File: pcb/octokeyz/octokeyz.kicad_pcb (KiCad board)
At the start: 2 copper layers, 84.6 x 36.3 mm, 30 parts, among them J1 USB, J2 ISP Programming, SW1 SW_Push, SW2 SW_Push, SW3 SW_Push, SW4 SW_Push, SW5 SW_Push, SW6 SW_Push, SW7 SW_Push, SW8 SW_Push, U1 ATtiny4313-P, Y1 20MHz

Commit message: pcb: octokeyz: revision 20240601
minor changes.
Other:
- board text added: "+5V OUT. ONLY!"
- board text added: "GND"
- board text added: "ISP"
- board text added: "MISO"
- board text added: "MOSI"
- board text added: "RESET"
- board text added: "SCK"
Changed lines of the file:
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@@
 	(title_block
 		(title "octokeyz")
-		(date "2024-05-30")
-		(rev "20240530")
+		(date "2024-06-01")
+		(rev "20240601")
 		(comment 3 "Released under CERN Open Hardware Licence Version 2 - Strongly Reciprocal")
 		(comment 4 "Designed by: Rafael G. Martins")
@@
 			)
 		)
-		(fp_text user "K"
-			(at 0 -1.8 90)
+		(fp_text user "${REFERENCE}"
+			(at 4.11 0 90)
 			(layer "F.Fab")
 			(effects
 				(font
-					(size 1 1)
-					(thickness 0.15)
+					(size 0.8 0.8)
+					(thickness 0.12)
 				)
 			)
 		)
-		(fp_text user "${REFERENCE}"
-			(at 4.11 0 90)
+		(fp_text user "K"
+			(at 0 -1.8 90)
 			(layer "F.Fab")
 			(effects
 				(font
-					(size 0.8 0.8)
-					(thickness 0.12)
+					(size 1 1)
+					(thickness 0.15)
 				)
 			)
@@
 		(tags "Through hole angled pin header THT 1x06 2.54mm single row")
 		(property "Reference" "J2"
-			(at 4 3.2 180)
+			(at 2.724 3.175 180)
 			(layer "B.SilkS")
 			(effects
@@
 					(thickness 0.15)
 				)
-				(justify mirror)
+				(justify left mirror)
 			)
 		)
@@
 			(layer "B.Fab")
 		)
-		(fp_text user "MOSI"
-			(at 7.95 -11.85 0)
-			(unlocked yes)
-			(layer "B.SilkS")
-			(effects
-				(font
-					(size 0.6 0.6)
-					(thickness 0.15)
-				)
-				(justify left mirror)
-			)
-		)
-		(fp_text user "GND"
-			(at 8.25 -1.65 0)
-			(unlocked yes)
-			(layer "B.SilkS")
-			(effects
-				(font
-					(size 0.6 0.6)
-					(thickness 0.15)
-				)
-				(justify left mirror)
-			)
-		)
-		(fp_text user "+5V"
-			(at 8.15 0.9 0)
-			(unlocked yes)
-			(layer "B.SilkS")
-			(effects
-				(font
-					(size 0.6 0.6)
-					(thickness 0.15)
-				)
-				(justify left mirror)
-			)
-		)
-		(fp_text user "SCK"
-			(at 8.3 -6.75 0)
-			(unlocked yes)
-			(layer "B.SilkS")
-			(effects
-				(font
-					(size 0.6 0.6)
-					(thickness 0.15)
-				)
-				(justify left mirror)
-			)
-		)
-		(fp_text user "RESET"
-			(at 7.35 -9.3 0)
-			(unlocked yes)
-			(layer "B.SilkS")
-			(effects
-				(font
-					(size 0.6 0.6)
-					(thickness 0.15)
-				)
-				(justify left mirror)
-			)
-		)
-		(fp_text user "ISP"
-			(at 3.15 2.05 0)
-			(unlocked yes)
-			(layer "B.SilkS")
-			(effects
-				(font
-					(size 0.6 0.6)
-					(thickness 0.15)
-				)
-				(justify left mirror)
-			)
-		)
-		(fp_text user "MISO"
-			(at 7.95 -4.2 0)
-			(unlocked yes)
-			(layer "B.SilkS")
-			(effects
-				(font
-					(size 0.6 0.6)
-					(thickness 0.15)
-				)
-				(justify left mirror)
-			)
-		)
 		(fp_text user "${REFERENCE}"
 			(at 2.77 -6.35 -90)
@@
 		(layer "Edge.Cuts")
 	)
+	(gr_text "+5V\nOUT. ONLY!"
+		(at 113.665 73.787 0)
+		(layer "B.SilkS")
+		(effects
+			(font
+				(size 0.6 0.6)
+				(thickness 0.15)
+			)
+			(justify right mirror)
+		)
+	)
+	(gr_text "MISO"
+		(at 113.665 79.375 0)
+		(layer "B.SilkS")
+		(effects
+			(font
+				(size 0.6 0.6)
+				(thickness 0.15)
+			)
+			(justify right mirror)
+		)
+	)
+	(gr_text "RESET"
+		(at 113.665 84.455 0)
+		(layer "B.SilkS")
+		(effects
+			(font
+				(size 0.6 0.6)
+				(thickness 0.15)
+			)
+			(justify right mirror)
+		)
+	)
+	(gr_text "SCK"
+		(at 113.665 81.915 0)
+		(layer "B.SilkS")
+		(effects
+			(font
+				(size 0.6 0.6)
+				(thickness 0.15)
+			)
+			(justify right mirror)
+		)
+	)
+	(gr_text "ISP"
+		(at 121.158 73.152 0)
+		(layer "B.SilkS")
+		(effects
+			(font
+				(size 0.6 0.6)
+				(thickness 0.15)
+			)
+			(justify left mirror)
+		)
+	)
 	(gr_text "Rev: ${REVISION}"
 		(at 160.909 98.425 0)
@@
 		)
 	)
+	(gr_text "MOSI"
+		(at 113.665 86.995 0)
+		(layer "B.SilkS")
+		(effects
+			(font
+				(size 0.6 0.6)
+				(thickness 0.15)
+			)
+			(justify right mirror)
+		)
+	)
+	(gr_text "GND"
+		(at 113.665 76.835 0)
+		(layer "B.SilkS")
+		(effects
+			(font
+				(size 0.6 0.6)
+				(thickness 0.15)
+			)
+			(justify right mirror)
+		)
+	)

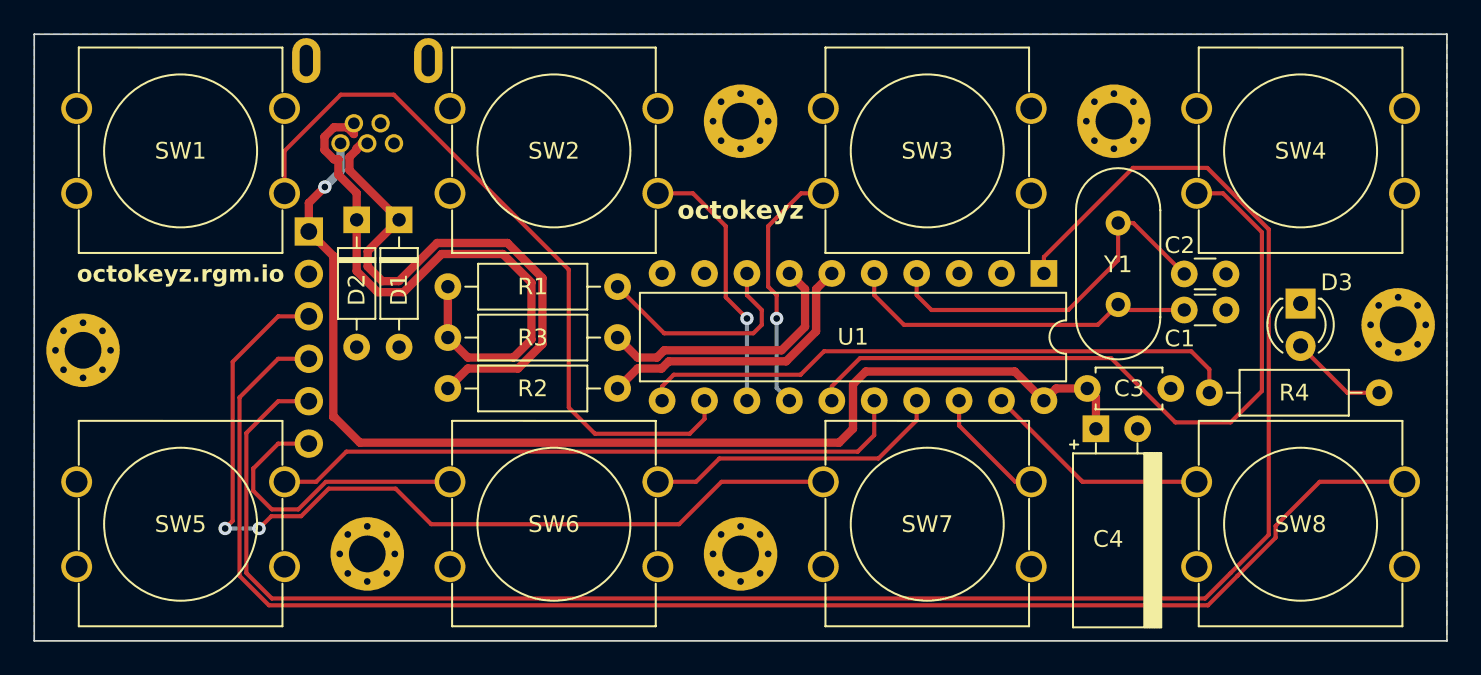
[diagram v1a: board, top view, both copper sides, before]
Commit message: pcb: octokeyz: revision 20240616
use stm32 instead of avr microcontroller. the prices are similar
nowadays, and it will allow us to have a single DFU-capable and
BSD-licensed firmware usable by all boards.

the board outline and the position of buttons and connectors is the
same, any existing cases should still fit correctly.
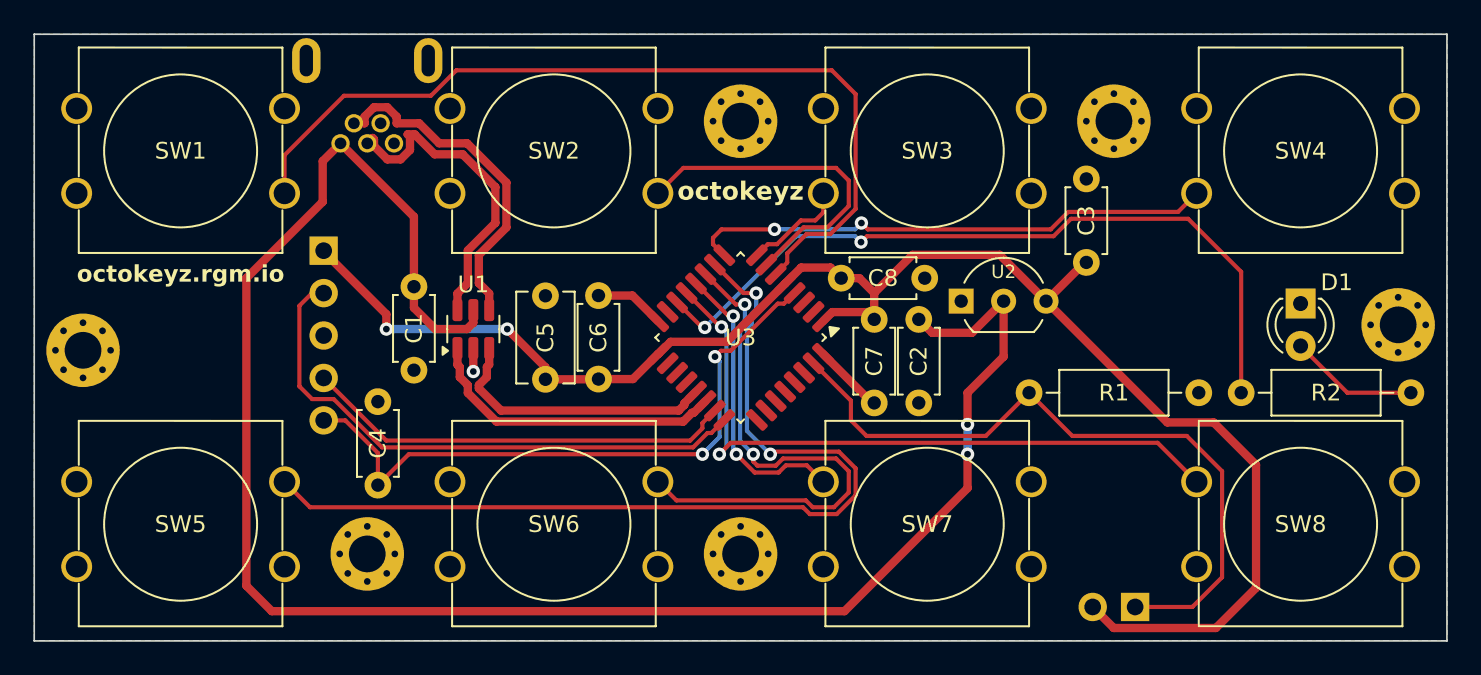
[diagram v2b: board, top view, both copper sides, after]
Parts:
- removed the D1 at (129.3, 74.5)
- removed D2: 3V6, Diode_THT:D_DO-35_SOD27_P7.62mm_Horizontal
- removed the R2 at (132.2, 84.6)
- removed R3: 68R, octokeyz:R_YAGEO_MFR-25FTE52_Horizontal
- removed Y1: 20MHz, Crystal:Crystal_HC49-4H_Vertical
- added C5: 10u, octokeyz:C_TDK_FA26, F.Cu at (138.0, 79.0)
- added C6: 100n, octokeyz:C_TDK_FA28, F.Cu at (141.2, 79.0)
- added C7: 100n, octokeyz:C_TDK_FA28, F.Cu at (157.7, 85.4)
- added C8: 100n, octokeyz:C_TDK_FA28, F.Cu at (160.8, 78.0)
- added JP1: BOOT, Connector_PinHeader_2.54mm:PinHeader_1x02_P2.54mm_Horizontal, B.Cu at (173.4, 97.7)
- added U2: MCP1700-3302E, Package_TO_SOT_THT:TO-92_Inline_Wide, F.Cu at (162.9, 79.4)
- added U3: STM32F042K6T6, Package_QFP:LQFP-32_7x7mm_P0.8mm, F.Cu at (149.7, 81.5)
- C1: value 22p -> 100n; footprint Capacitor_THT:C_Disc_D3.0mm_W1.6mm_P2.50mm -> octokeyz:C_TDK_FA28
- C2: value 22p -> 1u; footprint Capacitor_THT:C_Disc_D3.0mm_W1.6mm_P2.50mm -> octokeyz:C_TDK_FA28
- C3: value 100n -> 1u
- C4: value 10u -> 100n; footprint octokeyz:CP_Radial_D5.0mm_P2.50mm_Horizontal -> octokeyz:C_TDK_FA28
- D1: renamed from D3; value LED -> LED Green 3mm
- J1: value USB -> USB_B_Mini
- J2: value ISP Programming -> PIN H 5P; footprint Connector_PinHeader_2.54mm:PinHeader_1x06_P2.54mm_Horizontal -> Connector_PinHeader_2.54mm:PinHeader_1x05_P2.54mm_Horizontal
- R1: value 2k2 -> 10k
- R2: renamed from R4; value 22k -> 10k
- SW1, SW2, SW3, SW4, SW5, SW6, SW7, SW8: value SW_Push -> SPST 12mm
- U1: value ATtiny4313-P -> USBLC6-2SC6; footprint Package_DIP:DIP-20_W7.62mm -> Package_TO_SOT_SMD:SOT-23-6
- moved C1 48.8 mm to (130.2, 83.5), turned to 90 degrees
- moved C4 43.0 mm to (128.0, 85.4), turned to -90 degrees
- moved R1 35.4 mm to (167.0, 84.8)
- moved U1 34.3 mm to (133.7, 81.0), turned to 90 degrees
- moved C2 19.9 mm to (160.4, 85.4), turned to 90 degrees
- moved C3 13.5 mm to (170.4, 72.0), turned to -90 degrees
- moved R2 1.91 mm to (179.7, 84.8)
- moved J2 1.45 mm to (124.8, 76.3)
- moved REF** 0.06 mm to (183.3, 70.4)
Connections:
- C1 pad 2: Net-(U1-PA0/XTAL1) -> +5V
- C2 pad 2: Net-(U1-PA1/XTAL2) -> +5V
- C3 pad 2: +5V -> +3.3V
- C4 pad 1: +5V -> GND
- C4 pad 2: GND -> RESET
- J2 pad 1: +5V -> +3.3V
- J2 pad 2: GND -> SWCLK
- J2 pad 3: MISO -> GND
- J2 pad 4: SCK -> SWDIO
- R1 pad 1: /USB_CONN_D- -> Net-(JP1-A)
- R1 pad 2: USB_PULLUP -> GND
- SW1 pad 4: Net-(U1-PB0) -> KEY1
- SW2 pad 4: Net-(U1-PB1) -> KEY2
- SW3 pad 3: Net-(U1-PB2) -> KEY3
- SW4 pad 3: Net-(U1-PB3) -> KEY4
- SW5 pad 2: Net-(U1-PB4) -> KEY5
- SW6 pad 1: MOSI -> unconnected-(SW6-Pad1)
- SW6 pad 2: Net-(U1-PB5) -> KEY6
- SW7 pad 1: MISO -> KEY7
- SW7 pad 2: Net-(U1-PB6) -> unconnected-(SW7-Pad2)
- SW8 pad 1: Net-(U1-PB7) -> KEY8
- SW8 pad 2: SCK -> unconnected-(SW8-Pad2)
- U1 pad 1: RESET -> USB_D+
- U1 pad 2: unconnected-(U1-PD0-Pad2) -> GND
- U1 pad 3: unconnected-(U1-PD1-Pad3) -> USB_D-
- U1 pad 4: Net-(U1-PA1/XTAL2) -> /USB_CONN_D-
- U1 pad 5: Net-(U1-PA0/XTAL1) -> +5V
- U1 pad 6: USB_D+ -> /USB_CONN_D+
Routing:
- net +3.3V: track 0.00 -> 96.9 mm, vias 0 -> 2
- net SCK: track 89.5 -> 0.00 mm
- net RESET: track 112.6 -> 38.9 mm, vias 0 -> 2
- net KEY5: track 0.00 -> 56.3 mm, vias 0 -> 2
- net MISO: track 54.3 -> 0.00 mm, vias 2 -> 0
- net KEY1: track 0.00 -> 52.8 mm
- net Net-(U1-PB3): track 44.1 -> 0.00 mm
- net Net-(U1-PB0): track 43.8 -> 0.00 mm
- net Net-(JP1-A): track 0.00 -> 42.3 mm
- net KEY8: track 0.00 -> 40.7 mm, vias 0 -> 2
- net +5V: track 70.5 -> 110.6 mm, vias 1 -> 2
- net Net-(U1-PB4): track 38.5 -> 0.00 mm
- net SWCLK: track 0.00 -> 34.2 mm
- net KEY6: track 0.00 -> 33.0 mm, vias 0 -> 2
- net KEY4: track 0.00 -> 31.7 mm, vias 0 -> 2
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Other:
- board text added: "+3.3V OUT. ONLY!"
- board text added: "Boot to DFU"
- board text added: "SWCLK"
- board text added: "SWD"
- board text added: "SWDIO"
- board text removed: "+5V OUT. ONLY!"
- board text removed: "ISP"
- board text removed: "MISO"
- board text removed: "MOSI"
- board text removed: "SCK"

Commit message: pcb: added STM32F042K4T6 as microcontroller alternative
as this is a purely cosmetic change that doesn't affects the produced
boards I do not bumped revision number neither re-generated gerber
files.
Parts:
- U3: value STM32F042K6T6 -> STM32F042K4T6 or STM32F042K6T6

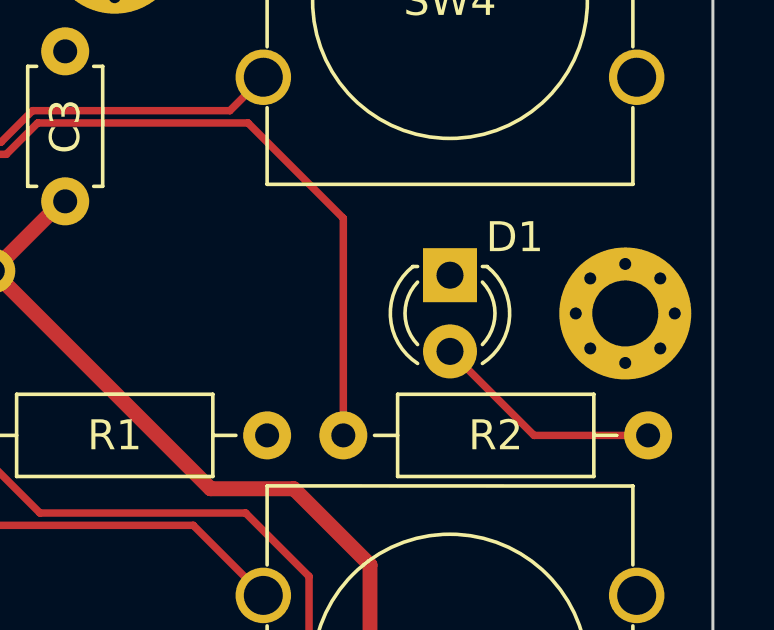
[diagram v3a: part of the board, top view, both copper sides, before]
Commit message: pcb: upgrade to kicad 9
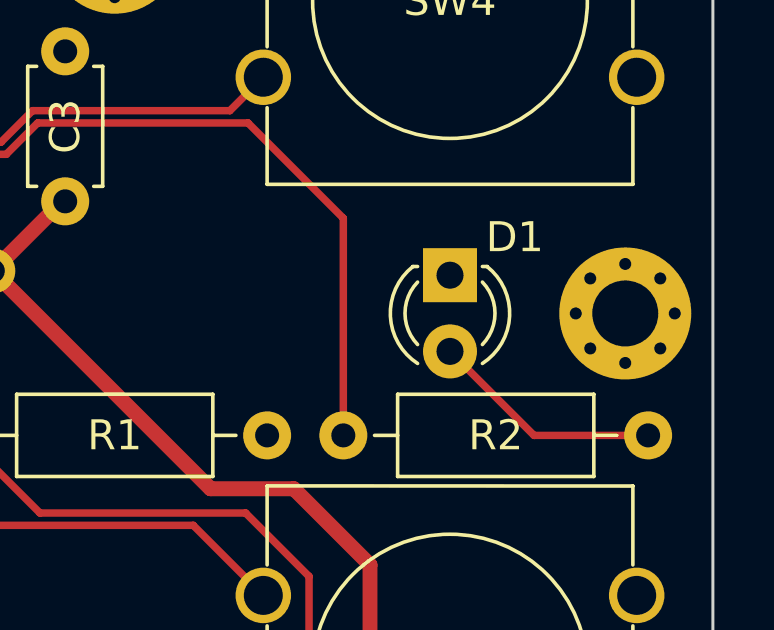
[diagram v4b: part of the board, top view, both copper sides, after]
